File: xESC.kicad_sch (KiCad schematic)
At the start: 16 parts, among them U10 xESC2, U20 2.54mm 2x2 socket, U23 2.54mm 2x2 socket, U26 2.54mm 2x2 socket, U32 2.54mm 1x6 socket, U35 2.54mm 1x6 socket, U38 2.54mm 1x9 socket, U41 2.54mm 1x5 socket

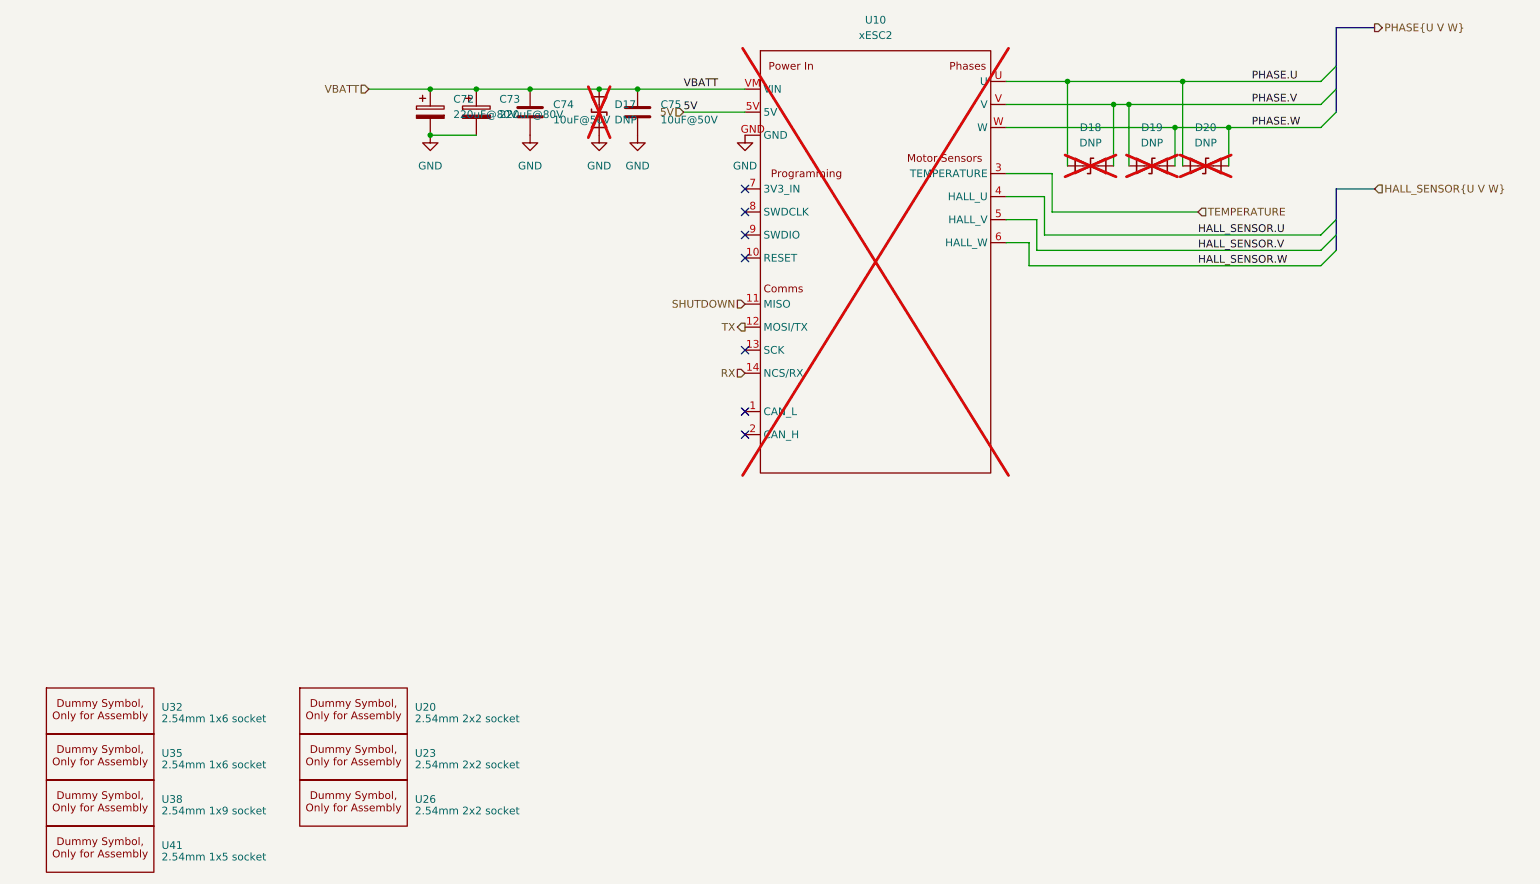
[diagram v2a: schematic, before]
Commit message: Make ERC happy
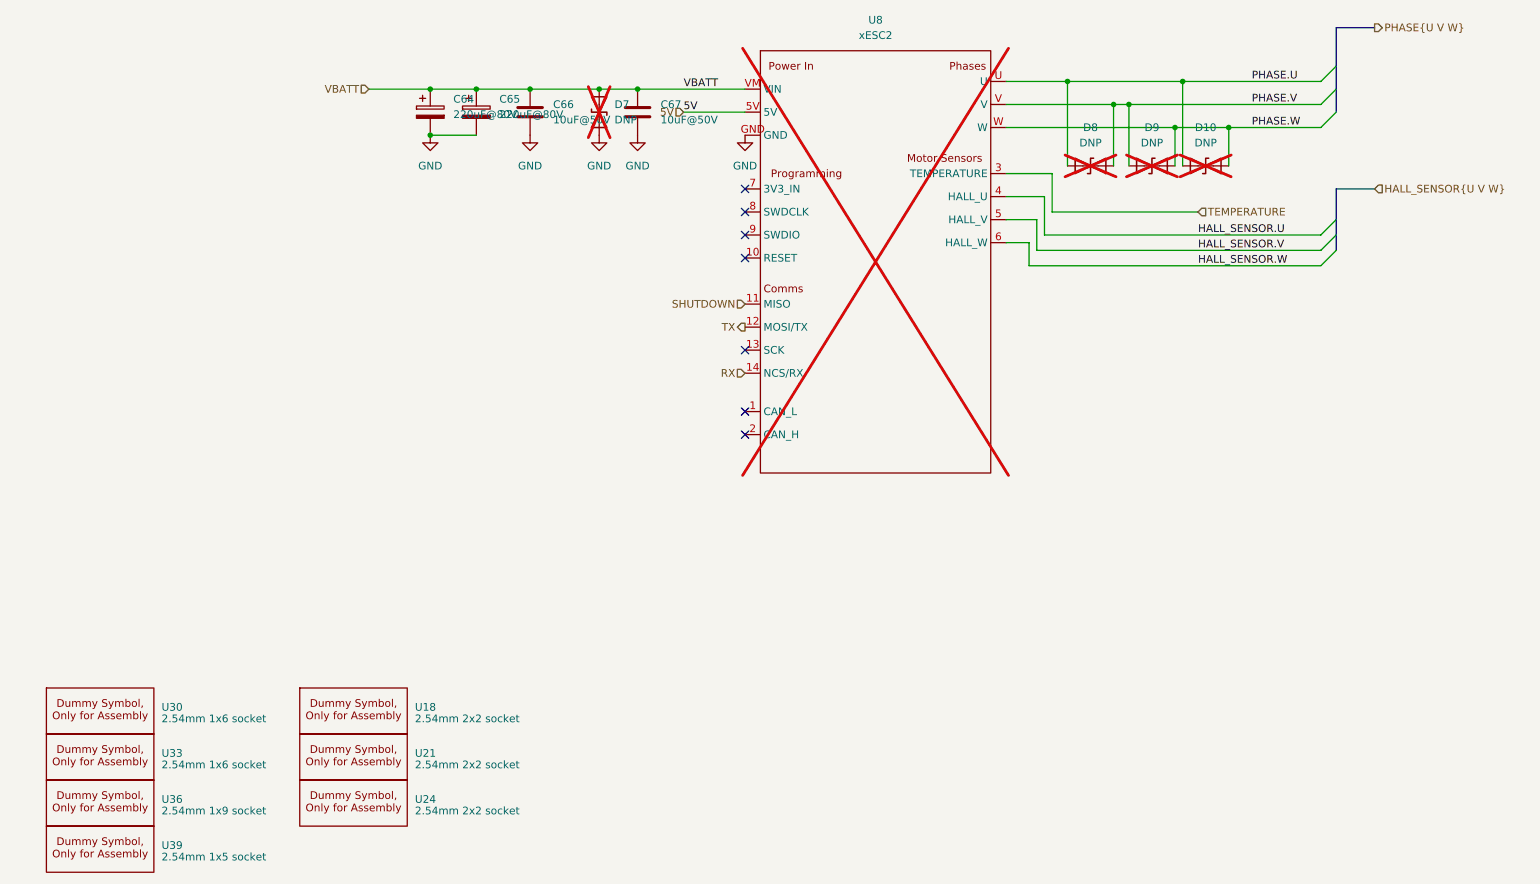
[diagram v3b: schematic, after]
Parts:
- renumbered C72 to C64, C73 to C65, C74 to C66, C75 to C67, D20 to D10, D17 to D7, D18 to D8, D19 to D9, U20 to U18, U23 to U21, U26 to U24, U32 to U30, U35 to U33, U38 to U36, U41 to U39, U10 to U8
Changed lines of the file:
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@@
 (kicad_sch
-	(version 20231120)
+	(version 20250114)
 	(generator "eeschema")
-	(generator_version "8.0")
+	(generator_version "9.0")
 	(paper "A3")
 	(junction
@@
 	(label "HALL_SENSOR.W"
 		(at 217.17 129.54 0)
-		(fields_autoplaced yes)
 		(effects
 			(font
@@
 	(label "PHASE.W"
 		(at 226.06 106.68 0)
-		(fields_autoplaced yes)
 		(effects
 			(font
@@
 	(label "HALL_SENSOR.U"
 		(at 217.17 124.46 0)
-		(fields_autoplaced yes)
 		(effects
 			(font
@@
 	(label "5V"
 		(at 132.08 104.14 0)
-		(fields_autoplaced yes)
 		(effects
 			(font
@@
 	(label "PHASE.V"
 		(at 226.06 102.87 0)
-		(fields_autoplaced yes)
 		(effects
 			(font
@@
 	(label "PHASE.U"
 		(at 226.06 99.06 0)
-		(fields_autoplaced yes)
 		(effects
 			(font
@@
 	(label "VBATT"
 		(at 132.08 100.33 0)
-		(fields_autoplaced yes)
 		(effects
 			(font
@@
 	(label "HALL_SENSOR.V"
 		(at 217.17 127 0)
-		(fields_autoplaced yes)
 		(effects
 			(font
@@
 		(shape output)
 		(at 246.38 90.17 0)
-		(fields_autoplaced yes)
 		(effects
 			(font
@@
 		(shape input)
 		(at 132.08 104.14 180)
-		(fields_autoplaced yes)
 		(effects
 			(font
@@
 		(shape input)
 		(at 142.24 147.32 180)
-		(fields_autoplaced yes)
 		(effects
 			(font
@@
 		(shape input)
 		(at 246.38 116.84 0)
-		(fields_autoplaced yes)
 		(effects
 			(font
@@
 		(shape input)
 		(at 217.17 120.65 0)
-		(fields_autoplaced yes)
 		(effects
 			(font
@@
 		(shape input)
 		(at 80.01 100.33 180)
-		(fields_autoplaced yes)
 		(effects
 			(font
@@
 		(shape input)
 		(at 142.24 135.89 180)
-		(fields_autoplaced yes)
 		(effects
 			(font
@@
 		(shape output)
 		(at 142.24 139.7 180)
-		(fields_autoplaced yes)
 		(effects
 			(font
@@
 		(dnp no)
 		(fields_autoplaced yes)
-		(property "Reference" "U41"
+		(property "Reference" "U39"
 			(at 45.72 225.4249 0)
 			(effects
@@
 		(dnp yes)
 		(fields_autoplaced yes)
-		(property "Reference" "D17"
+		(property "Reference" "D7"
 			(at 120.65 102.8699 90)
 			(effects
@@
 		(dnp yes)
 		(fields_autoplaced yes)
-		(property "Reference" "U10"
+		(property "Reference" "U8"
 			(at 163.83 88.9 0)
 			(effects
@@
 		(dnp yes)
 		(fields_autoplaced yes)
-		(property "Reference" "D20"
+		(property "Reference" "D10"
 			(at 218.44 106.68 0)
 			(effects
@@
 		(dnp no)
 		(fields_autoplaced yes)
-		(property "Reference" "U20"
+		(property "Reference" "U18"
 			(at 87.63 202.5649 0)
 			(effects
@@
 		(dnp no)
 		(fields_autoplaced yes)
-		(property "Reference" "C75"
+		(property "Reference" "C67"
 			(at 128.27 102.8699 0)
 			(effects
@@
 		(dnp no)
 		(fields_autoplaced yes)
-		(property "Reference" "U38"
+		(property "Reference" "U36"
 			(at 45.72 217.8049 0)
 			(effects
@@
 		(dnp no)
 		(fields_autoplaced yes)
-		(property "Reference" "#PWR0137"
+		(property "Reference" "#PWR0125"
 			(at 142.24 114.3 0)
 			(effects
@@
 		(dnp no)
 		(fields_autoplaced yes)
-		(property "Reference" "U35"
+		(property "Reference" "U33"
 			(at 45.72 210.1849 0)
 			(effects
@@
 		(dnp no)
 		(fields_autoplaced yes)
-		(property "Reference" "U32"
+		(property "Reference" "U30"
 			(at 45.72 202.5649 0)
 			(effects
@@
 		(dnp no)
 		(fields_autoplaced yes)
-		(property "Reference" "U23"
+		(property "Reference" "U21"
 			(at 87.63 210.1849 0)
 			(effects
@@
 		(dnp no)
 		(fields_autoplaced yes)
-		(property "Reference" "#PWR0134"
+		(property "Reference" "#PWR0122"
 			(at 106.68 114.3 0)
 			(effects
@@
 		(dnp no)
 		(fields_autoplaced yes)
-		(property "Reference" "C72"
+		(property "Reference" "C64"
 			(at 93.98 101.9809 0)
 			(effects
@@
 		(dnp yes)
 		(fields_autoplaced yes)
-		(property "Reference" "D18"
+		(property "Reference" "D8"
 			(at 199.39 106.68 0)
 			(effects
@@
 		(dnp no)
 		(fields_autoplaced yes)
-		(property "Reference" "C74"
+		(property "Reference" "C66"
 			(at 110.49 102.8699 0)
 			(effects
@@
 		(dnp no)
 		(fields_autoplaced yes)
-		(property "Reference" "C73"
+		(property "Reference" "C65"
 			(at 101.6 101.9809 0)
 			(effects
@@
 		(dnp no)
 		(fields_autoplaced yes)
-		(property "Reference" "U26"
+		(property "Reference" "U24"
 			(at 87.63 217.8049 0)
 			(effects
@@
 		(dnp no)
 		(fields_autoplaced yes)
-		(property "Reference" "#PWR0136"
+		(property "Reference" "#PWR0124"
 			(at 124.46 114.3 0)
 			(effects
@@
 		(dnp no)
 		(fields_autoplaced yes)
-		(property "Reference" "#PWR0135"
+		(property "Reference" "#PWR0123"
 			(at 118.11 114.3 0)
 			(effects
@@
 		(dnp no)
 		(fields_autoplaced yes)
-		(property "Reference" "#PWR0133"
+		(property "Reference" "#PWR0121"
 			(at 90.17 114.3 0)
 			(effects
@@
 		(dnp yes)
 		(fields_autoplaced yes)
-		(property "Reference" "D19"
+		(property "Reference" "D9"
 			(at 209.55 106.68 0)
 			(effects

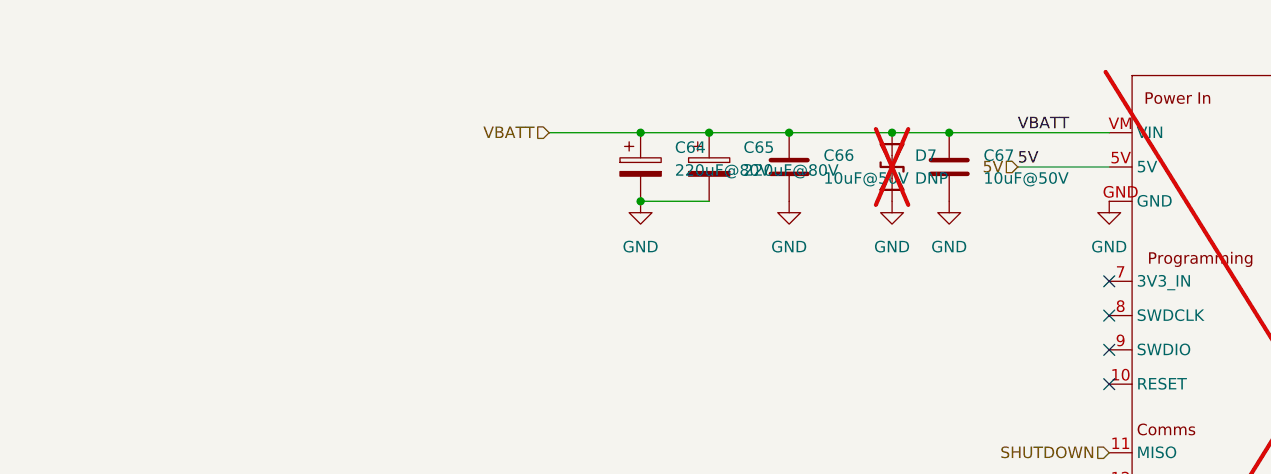
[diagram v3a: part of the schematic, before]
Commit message: V_BATT TVS protection
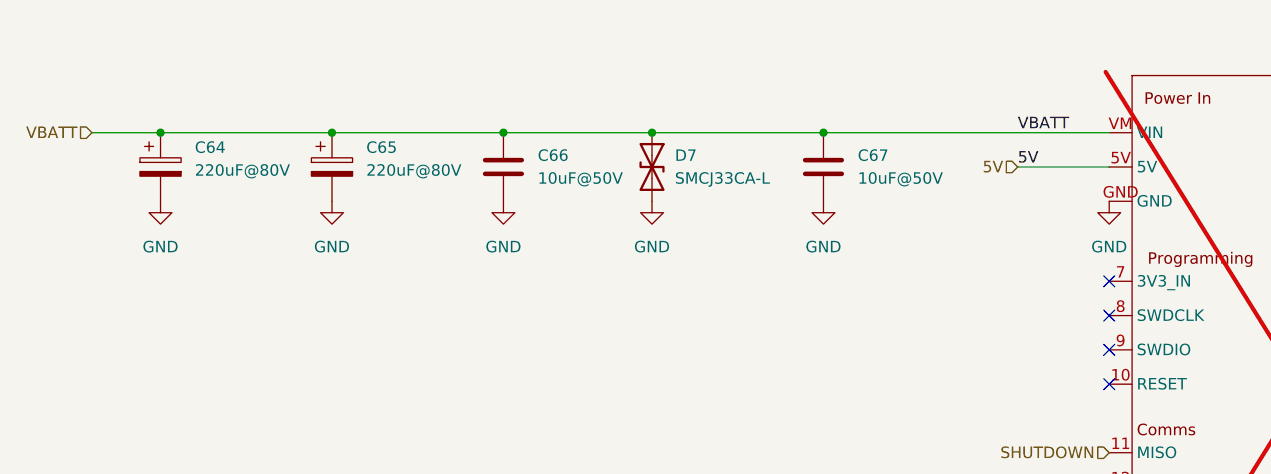
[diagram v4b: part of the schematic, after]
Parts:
- D7: value DNP -> SMCJ33CA-L; footprint Diode_SMD:D_SMA -> Diode_SMD:D_SMC; Config do not place -> (none); DNP Y -> (none); JLC (none) -> C7470408; now fitted
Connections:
- net GND: now also D7.2 (A2); no longer D7.1 (A1)
- net VBATT: now also D7.1 (A1); no longer D7.2 (A2)
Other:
- moved on the sheet: C64, C65, C66, C67
